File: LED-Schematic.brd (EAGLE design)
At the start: 160 x 100 mm, 12 parts, among them J1 POWER_JACKPTH, Q1 SUP75N06-08, Q2 SUP75N06-08, Q3 SUP75N06-08

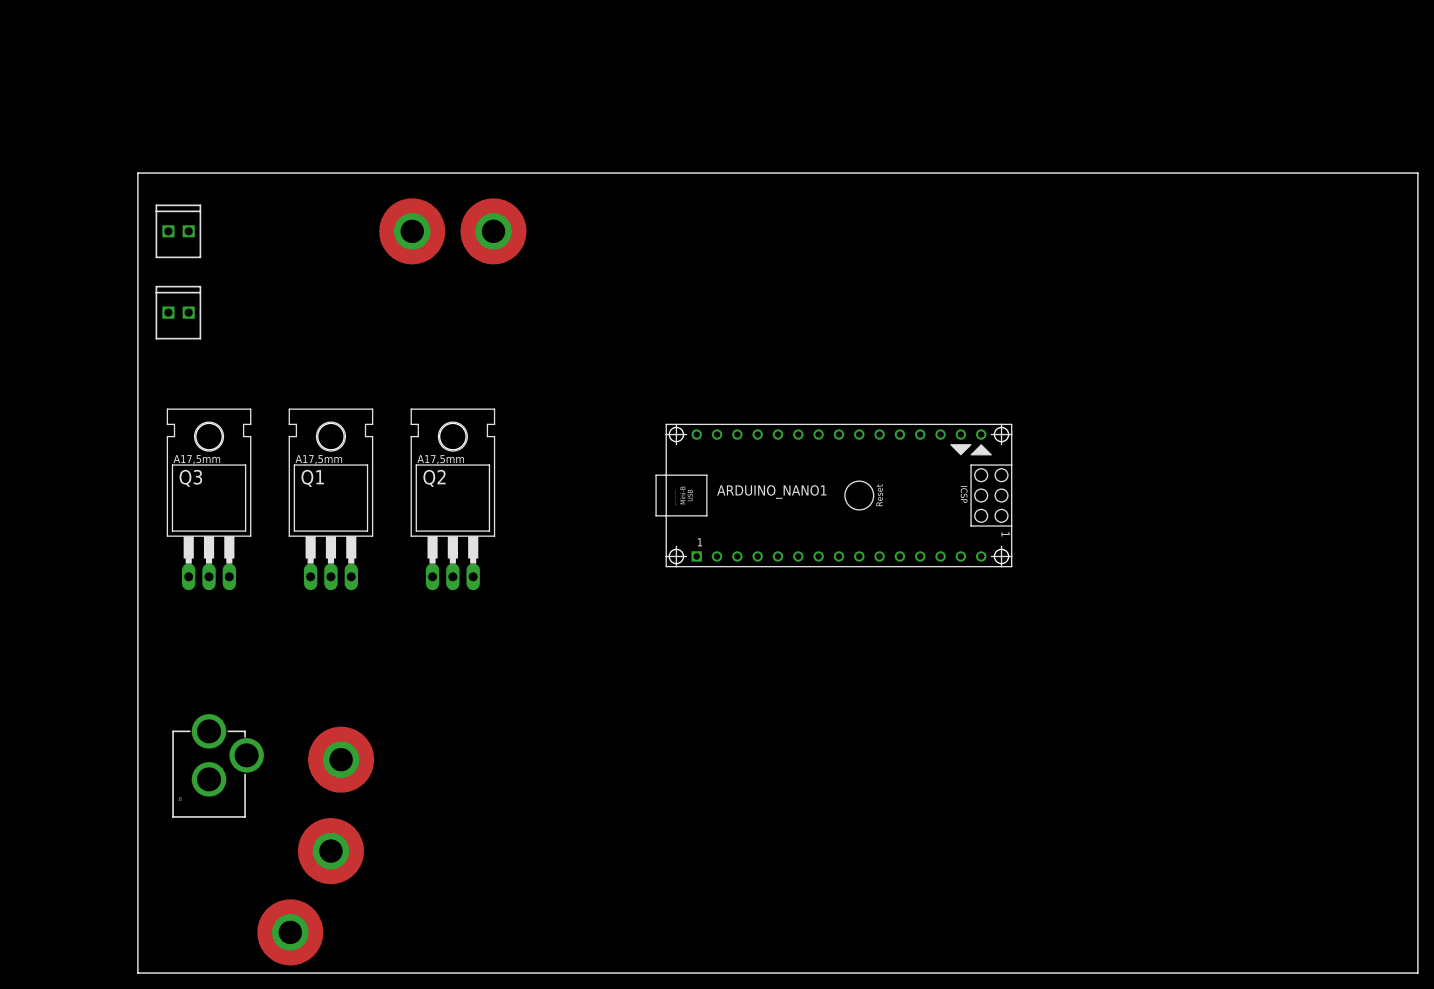
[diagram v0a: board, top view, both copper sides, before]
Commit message: Added arduino to schematic, added PCB board, added gitignore
Signed-off-by: Maximilian Pult <it@optik-riede.de>
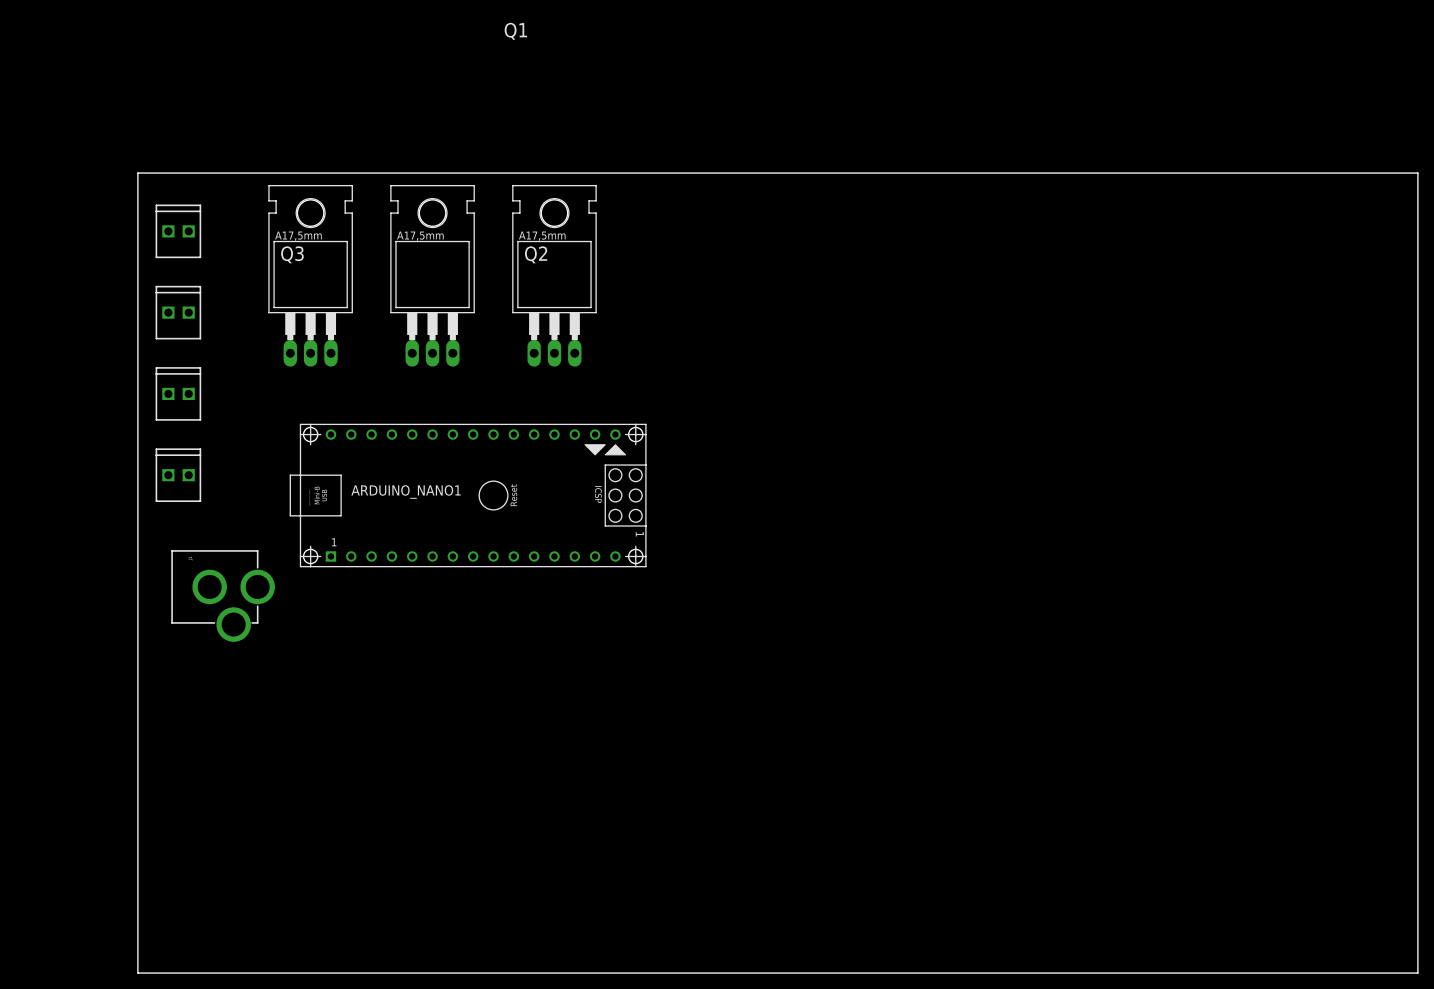
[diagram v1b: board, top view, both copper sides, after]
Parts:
- removed J6, J7, J8: (no value), SparkFun-Connectors:SNAP-FEMALE
- J4, J5: device SparkFun-Connectors:SNAP-FEMALE -> SparkFun-Connectors:1X02_2.54_SCREWTERM
- moved J5 59.1 mm to (3.81, 62.2)
- moved J4 50.6 mm to (3.81, 72.4)
- moved ARDUINO_NANO1 45.7 mm to (44.5, 59.7)
- moved J1 32.7 mm to (1.27, 48.3), turned to 270 degrees
- moved Q1 30.7 mm to (36.8, 83.8)
- moved Q2 30.7 mm to (52.1, 83.8)
- moved Q3 30.7 mm to (21.6, 83.8)
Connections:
- net B-OUT renamed B-LED
- net G-OUT renamed G-LED
- net R-OUT renamed R-LED
- removed net 5V: ARDUINO_NANO1.12
- removed net N$3: J1.GNDBREAK, J8.1, Q1.3, Q2.3, Q3.3
- removed net P-OUT: J1.PWR, J2.P1, J7.1
- removed net VIN: ARDUINO_NANO1.15
- new net ECHO-SENSE: ARDUINO_NANO1.29, J4.P1
- new net GND-SENSE: J5.P1
- new net P-LED: ARDUINO_NANO1.15, J1.PWR, J2.P1
- new net P-SENSE: ARDUINO_NANO1.12, J5.P2
- new net TRIG-SENSE: ARDUINO_NANO1.30, J4.P2
- net B-GATE: now also ARDUINO_NANO1.21; no longer J4.1
- net G-GATE: now also ARDUINO_NANO1.24; no longer J6.1
- net GND: now also J1.GNDBREAK, Q1.3, Q2.3, Q3.3
- net R-GATE: now also ARDUINO_NANO1.23; no longer J5.1

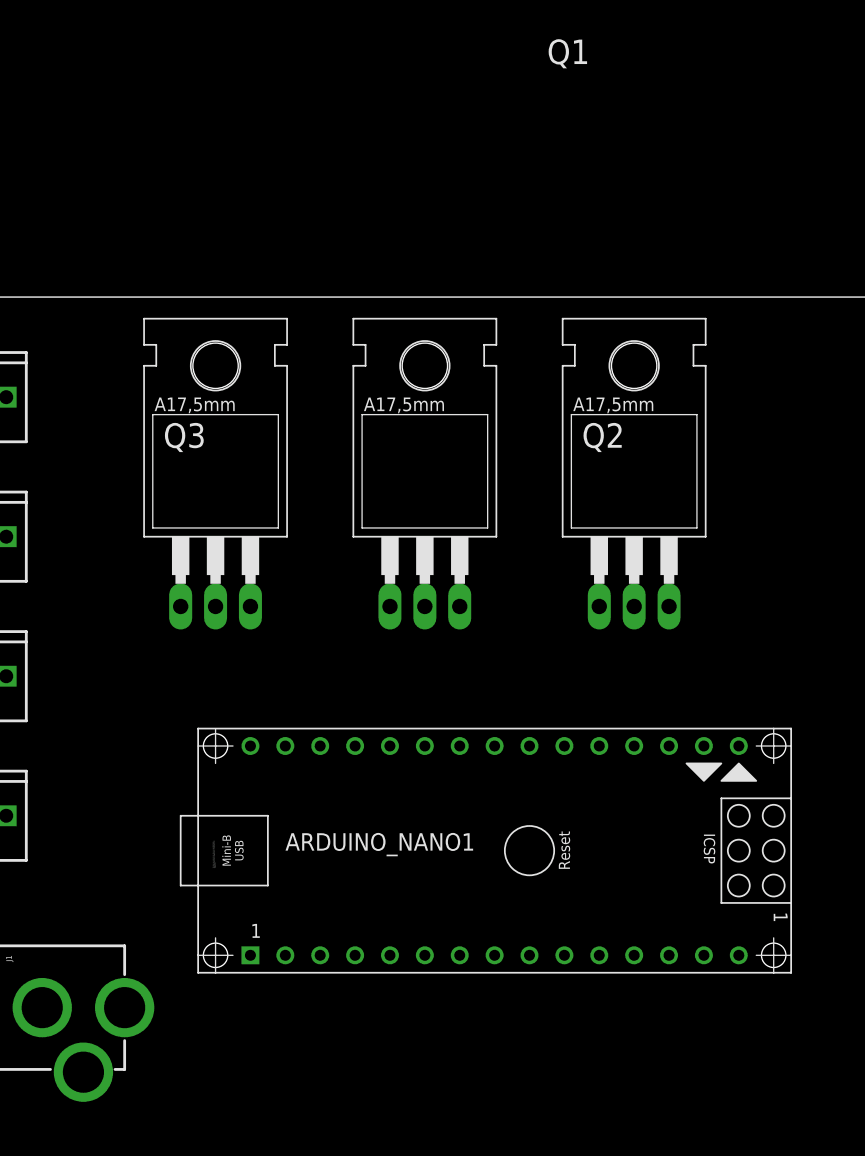
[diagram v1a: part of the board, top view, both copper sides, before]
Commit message: swapped mosfets to infineon IRLs
Signed-off-by: Maximilian Pult <it@optik-riede.de>
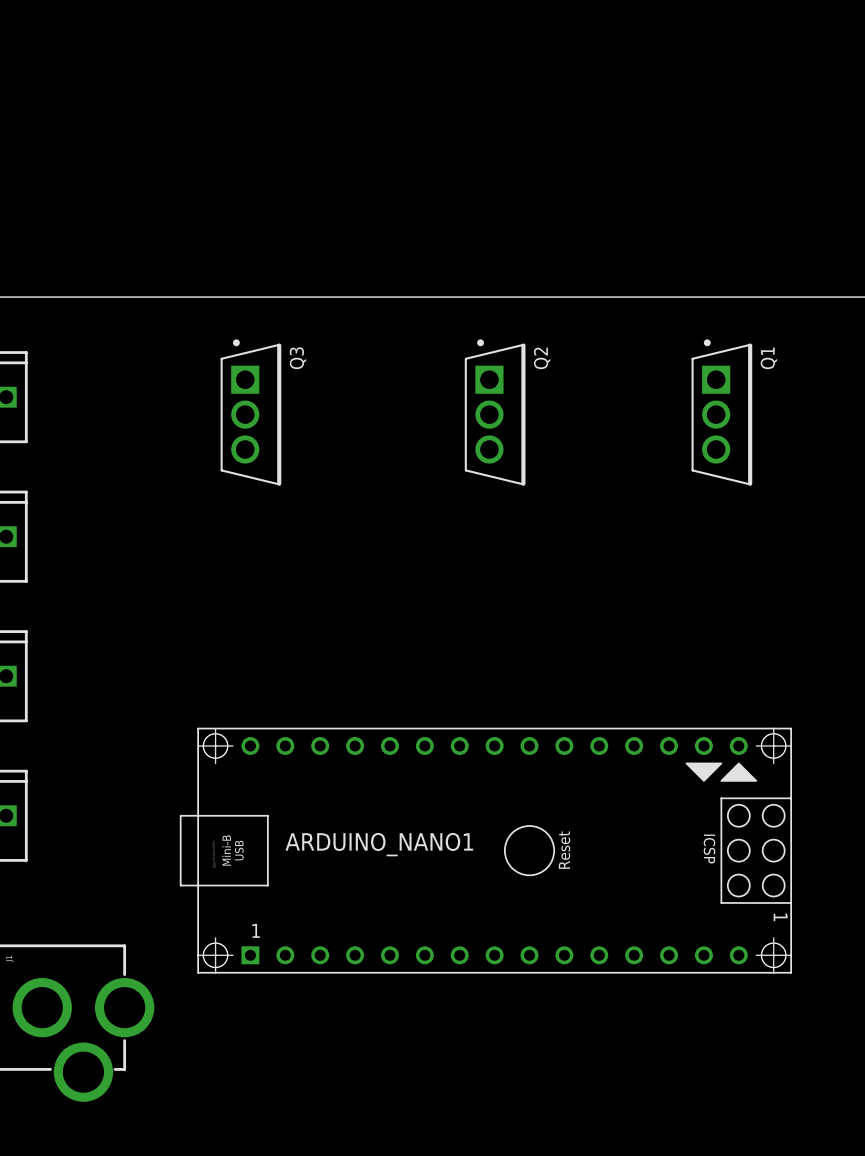
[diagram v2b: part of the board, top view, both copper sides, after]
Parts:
- J1: value POWER_JACKPTH -> POWER_JACK
- Q1, Q2, Q3: value SUP75N06-08 -> INFINEON_IRLB8721PBFINFINEON_IRLB8721PBF_0_0; device transistor-fet:TO220 -> Infineon - IRLB8721PbF:INFINEON_IRLB8721PBF_0
- moved Q1 22.9 mm to (58.4, 91.4)
- moved Q2 12.7 mm to (41.9, 91.4)
- moved Q3 8.03 mm to (24.1, 91.4)

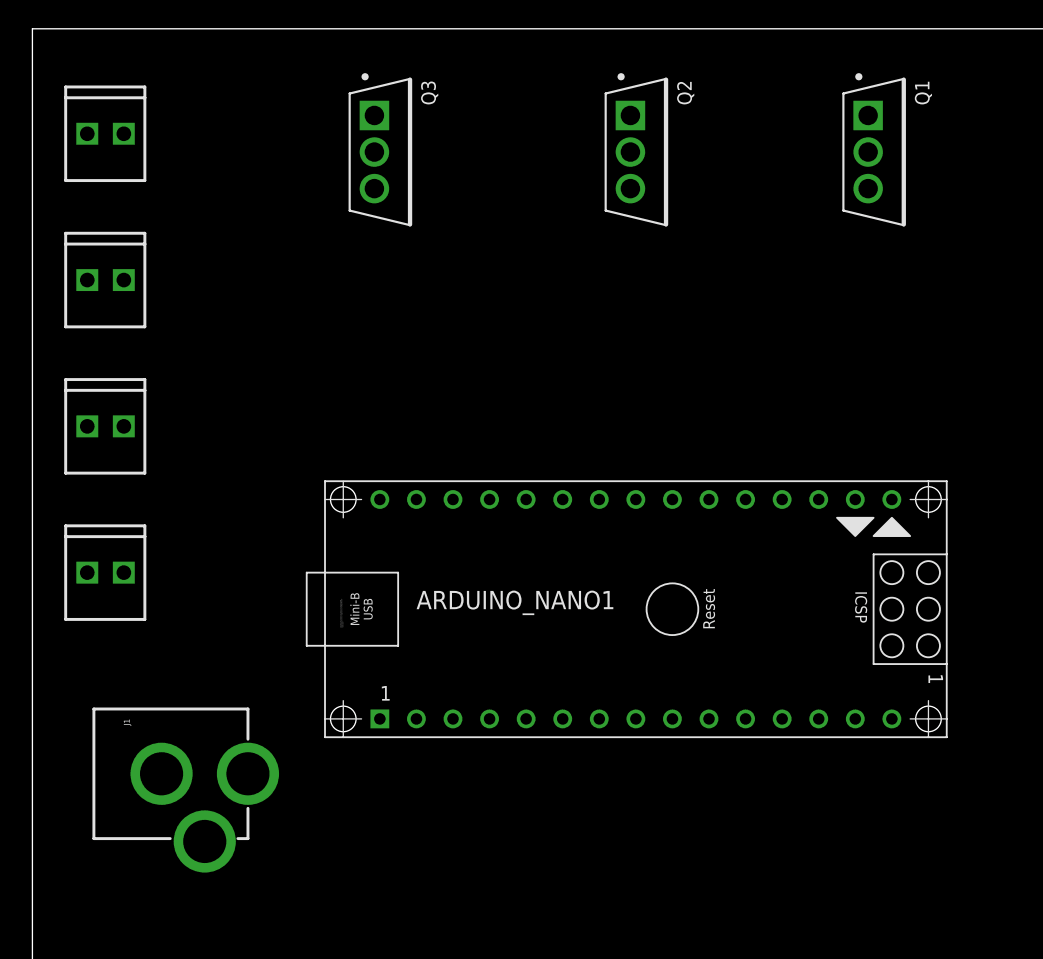
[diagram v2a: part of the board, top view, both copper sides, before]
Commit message: Adding Datasheets, replace screw terms
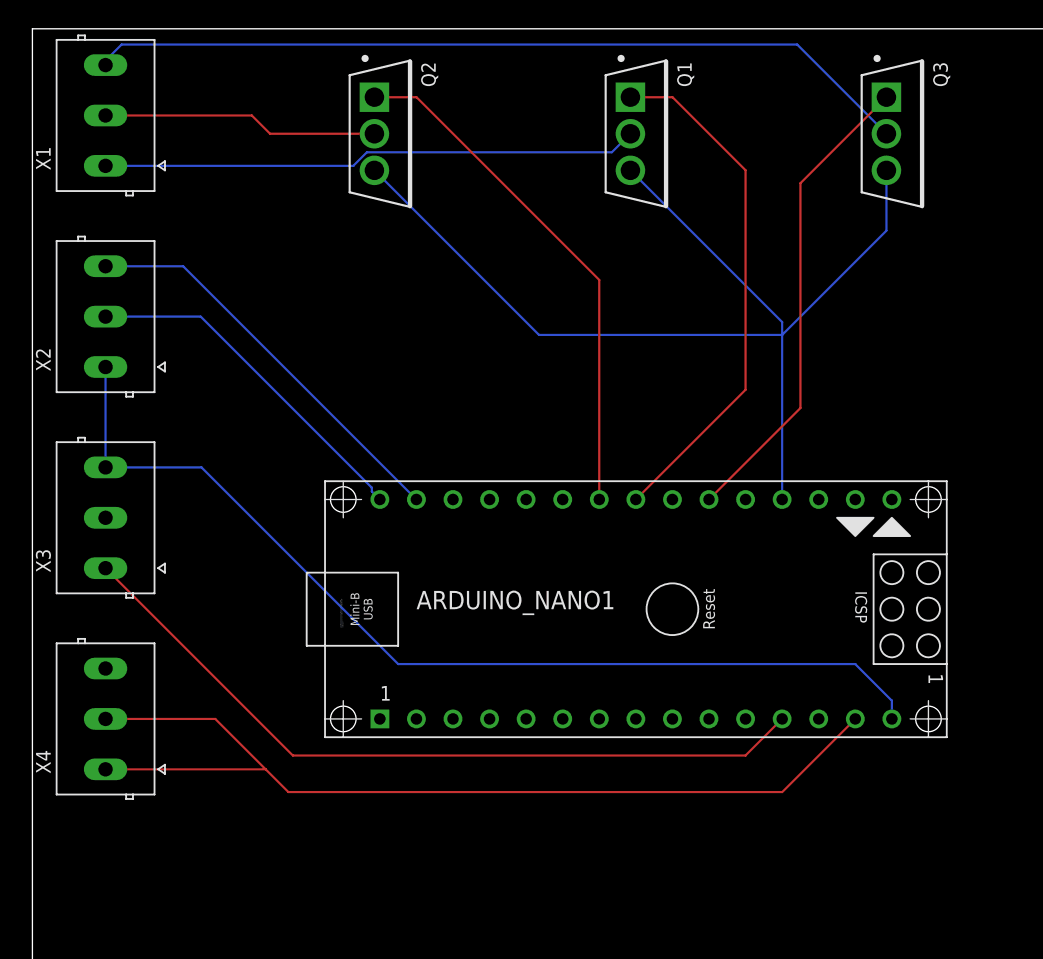
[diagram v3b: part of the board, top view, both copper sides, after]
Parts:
- removed J1: POWER_JACK, SparkFun-Connectors:POWER_JACK_PTH
- removed J2, J3, J4, J5: (no value), SparkFun-Connectors:1X02_2.54_SCREWTERM
- added X1, X2, X3, X4: DG3XX-03-3.5, degson:DG350-3.5-03P
- moved Q3 35.6 mm to (59.7, 92.7)
- moved Q2 17.8 mm to (24.1, 92.7)
- moved Q1 16.6 mm to (41.9, 92.7)
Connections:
- new net BTN-IN: X4.3
- net B-LED: now also X1.3; no longer J2.P2
- net ECHO-SENSE: now also X2.3; no longer J4.P1
- net G-LED: now also X1.2; no longer J3.P1
- net GND: now also X4.1, X4.2; no longer J1.GNDBREAK
- net GND-SENSE: now also X3.2; no longer J5.P1
- net P-LED: now also X2.1, X3.3; no longer J1.PWR, J2.P1
- net P-SENSE: now also X3.1; no longer J5.P2
- net R-LED: now also X1.1; no longer J3.P2
- net TRIG-SENSE: now also X2.2; no longer J4.P2
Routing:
- net GND: track 0.07 -> 142.1 mm
- net P-LED: track 0.19 -> 69.6 mm
- net B-LED: track 0.00 -> 57.3 mm
- net P-SENSE: track 0.00 -> 53.4 mm
- net R-LED: track 0.00 -> 37.4 mm
- net R-GATE: track 0.00 -> 36.1 mm
- net G-GATE: track 0.00 -> 36.1 mm
- net B-GATE: track 0.00 -> 33.0 mm
- net ECHO-SENSE: track 0.00 -> 28.3 mm
- net TRIG-SENSE: track 0.00 -> 24.5 mm
- net G-LED: track 0.00 -> 19.2 mm

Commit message: Before reroute
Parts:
- moved X3 16.7 mm to (7.62, 49.5)
- moved X4 16.7 mm to (7.62, 35.6)
- moved X1 2.84 mm to (7.62, 92.7)
- moved X2 2.84 mm to (7.62, 78.7)
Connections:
- removed net GND-SENSE: X3.2
- net BTN-IN: now also ARDUINO_NANO1.26
- net GND: now also X3.2
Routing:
- net BTN-IN: track 0.00 -> 39.5 mm
- net GND: track 142.1 -> 176.6 mm
- net P-LED: track 69.6 -> 79.6 mm
- net P-SENSE: track 53.4 -> 47.0 mm
- net TRIG-SENSE: track 24.5 -> 21.4 mm
- net G-LED: track 19.2 -> 16.1 mm
- net ECHO-SENSE: track 28.3 -> 25.2 mm
- net R-LED: track 37.4 -> 35.4 mm
- net B-LED: track 57.3 -> 55.4 mm
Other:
- board text added: "BTN-IN"
